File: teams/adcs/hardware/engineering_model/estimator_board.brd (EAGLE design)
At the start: 90 x 90 mm, 58 parts, among them U1 Value, U2 Value

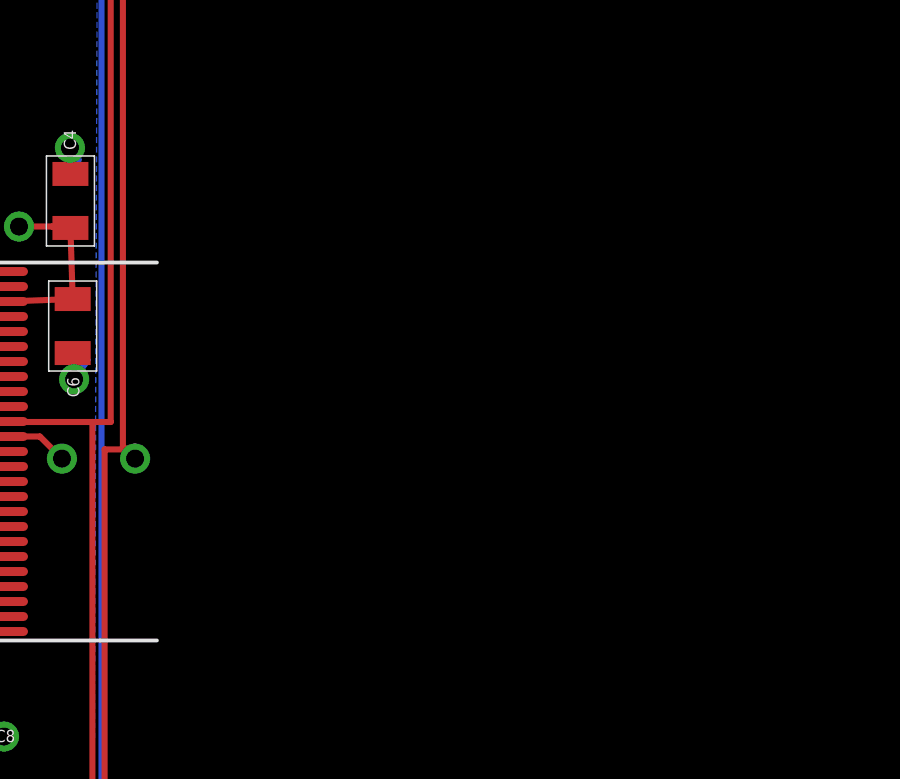
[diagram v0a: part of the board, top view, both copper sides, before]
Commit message: ADCS/Estimator: Add LSM6DSM to estimator board (unconnected)
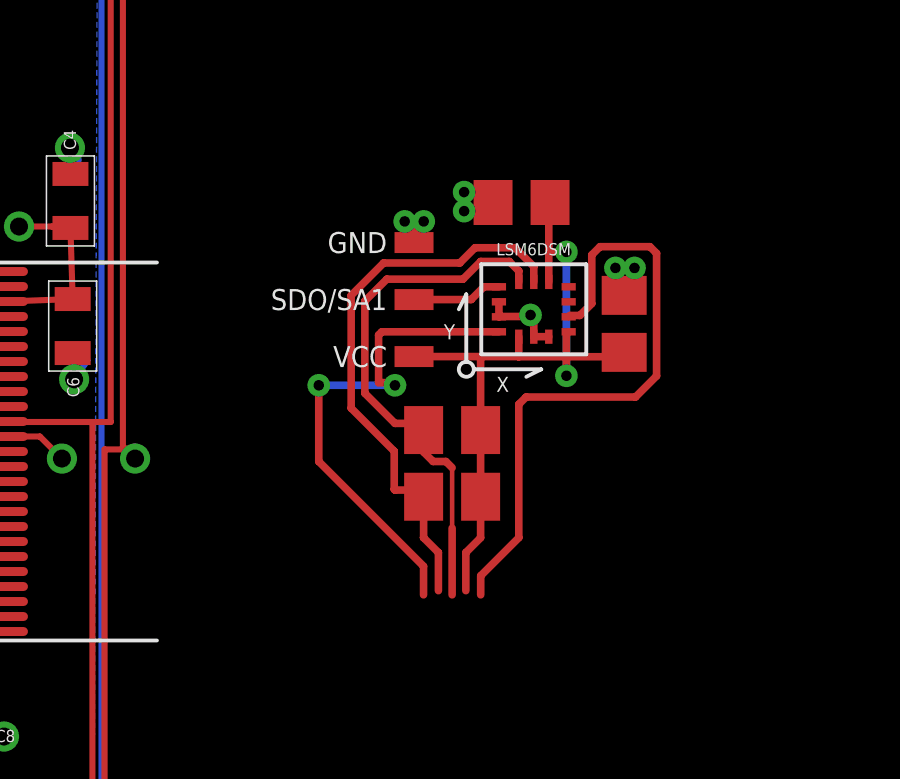
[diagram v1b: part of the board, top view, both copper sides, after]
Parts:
- added C24, C25: 0.1 μF, rcl:C0805
- added R10, R9: 10 kΩ, rcl:M0805
- added SDO/SA1: 0_OHM_JUMPER, DubSat1 Components:0_OHM_JUMPER
- added U$17: LSM6DSM, LSM6DSM:LSM6DSM
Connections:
- new net 3V3: C24.1, C25.2, R10.1, R9.1, SDO/SA1.P$3, U$17.CS, U$17.VDD, U$17.VDDIO
- new net IMU_INT1: U$17.INT1
- new net IMU_INT2: U$17.INT2
- new net IMU_SCL: R10.2, U$17.SCL
- new net IMU_SDA: R9.2, U$17.SDA
- new net N$25: SDO/SA1.P$2, U$17.SDO/SA0
- net GND: now also C24.2, C25.1, SDO/SA1.P$1, U$17.GND@1, U$17.GND@2, U$17.SCX, U$17.SDX
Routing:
- net 3V3: track 0.00 -> 24.6 mm, vias 0 -> 2
- net IMU_INT2: track 0.00 -> 20.9 mm
- net IMU_SCL: track 0.00 -> 19.0 mm
- net IMU_SDA: track 0.00 -> 18.1 mm
- net IMU_INT1: track 0.00 -> 17.2 mm, vias 0 -> 2
- net GND: track 65.1 -> 73.5 mm, vias 38 -> 45
- net N$25: track 0.00 -> 3.01 mm
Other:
- board text added: "LSM6DSM"

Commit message: finished estimator_board
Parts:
- removed L1: (no value), SparkFun-Passives:0805
- removed R4: 2.2KΩ, DubSat1 Components:0805
- added C22: 0.22µF, DubSat1 Components:0805
- added C23, C28: .1u, DubSat1 Components:0805
- added C26: 4.7u, DubSat1 Components:0805
- added C27: 1u, DubSat1 Components:0805
- added JP1, JP10, JP2, JP3, JP4, JP5, JP6, JP7, JP8, JP9: M02PTH, SparkFun-Connectors:1X02
- added R7: 2.2KΩ, DubSat1 Components:0805
- added U$18: HMC5983, DubSat1 Components:HMC5983
- R10, R9: value 10 kΩ -> 2.2KΩ; device rcl:M0805 -> DubSat1 Components:0805
- moved C21 13.2 mm to (27.0, -40.3), turned to 270 degrees
- moved SDO/SA1 13.0 mm to (-6.33, 16.1)
- moved C24 13.0 mm to (-2.75, 19.3)
- moved C25 13.0 mm to (0.67, 15.3)
- moved U$17 13.0 mm to (-2.34, 15.7)
- moved R9 11.6 mm to (-8.51, -12.0), turned to 0 degrees
- moved C17 9.86 mm to (25.6, -32.4), turned to 180 degrees
- moved U$15 9.55 mm to (26.7, -36.3), turned to 90 degrees
- moved R10 7.88 mm to (-8.51, -10.0), turned to 0 degrees
- moved R3 6.95 mm to (34.3, -14.2), turned to 180 degrees
- moved C18 4.49 mm to (29.3, -32.8), turned to 270 degrees
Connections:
- removed net 3V3: C24.1, C25.2, R10.1, R9.1, SDO/SA1.P$3, U$17.CS, U$17.VDD, U$17.VDDIO
- removed net IMU_SCL: R10.2, U$17.SCL
- removed net IMU_SDA: R9.2, U$17.SDA
- removed net N$23: C21.1, L1.2, R3.1, R4.1, U$15.!SPI_CS, U$15.I2C/!SPI, U$15.VDD, U$15.VDDIO
- new net N$22: JP10.2, U$15.DRDY
- new net N$26: JP3.2, U$18.SCL/SPI_SCK
- new net N$27: JP6.1, R7.2, U$7.P5.1_I2C-SCL-1
- new net N$28: JP5.2, R3.2, U$7.P5.0_I2C-SDA-1
- new net N$29: JP8.2, U2.62
- new net N$30: JP7.1, U2.61
- new net N$31: JP10.1, U$7.P1.7_GPIO/PWM
- new net N$32: JP9.2, U2.63
- new net N$34: C26.1, U$18.C1
- new net N$35: C22.2, U$18.SETP
- new net N$36: C22.1, U$18.SETC
- new net N$38: JP7.2, U$18.DRDY
- net 3.3V: now also C23.1, C24.1, C25.2, C27.1, C28.1, R10.1, R9.1, SDO/SA1.P$3, U$17.CS, U$17.VDD, U$17.VDDIO, U$18.!SPI_CS, U$18.I2C/!SPI, U$18.VDD, U$18.VDDIO
- net 3.3V-ISO: now also C21.1, R3.1, R7.1, U$15.!SPI_CS, U$15.I2C/!SPI, U$15.VDD, U$15.VDDIO; no longer L1.1
- net GND: now also C23.2, C26.2, C27.2, C28.2, U$18.GND, U$18.SOC
- net I2C_SCL2: now also JP2.1, JP2.2, JP3.1, R10.2, U$17.SCL
- net I2C_SDA2: now also JP1.1, JP1.2, JP4.1, JP4.2, R9.2, U$17.SDA, U$18.SDA/SPI_SDI
- net IMU_INT1: now also JP9.1
- net IMU_INT2: now also JP8.1
- net N$16: now also JP5.1; no longer R4.2, U$7.P5.0_I2C-SDA-1
- net N$18: now also JP6.2; no longer R3.2, U$7.P5.1_I2C-SCL-1
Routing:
- net 3.3V: track 49.6 -> 172.9 mm, vias 12 -> 20
- net I2C_SDA2: track 32.3 -> 112.0 mm, vias 1 -> 4
- net I2C_SCL2: track 30.4 -> 97.3 mm, vias 1 -> 3
- net 3.3V-ISO: track 110.2 -> 174.7 mm, vias 3 -> 7
- net N$23: track 32.5 -> 0.00 mm, vias 2 -> 0
- net N$27: track 0.00 -> 32.4 mm, vias 0 -> 2
- net N$28: track 0.00 -> 29.4 mm, vias 0 -> 2
- net 3V3: track 24.6 -> 0.00 mm, vias 2 -> 0
- net N$31: track 0.00 -> 21.5 mm, vias 0 -> 1
- net N$22: track 0.00 -> 19.8 mm
- net IMU_SCL: track 19.0 -> 0.00 mm
- net N$38: track 0.00 -> 18.9 mm
- net IMU_SDA: track 18.1 -> 0.00 mm
- net N$30: track 0.00 -> 16.2 mm
- net N$26: track 0.00 -> 15.7 mm
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- removed copper zone on layer 2, net N$24
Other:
- board text added: "DRDY"
- board text added: "IMU"
- board text added: "INT1"
- board text added: "INT2"
- board text added: "SCL"
- board text added: "SDA"
- board text added: "mag."
- board text removed: "add d_ready and soc"
